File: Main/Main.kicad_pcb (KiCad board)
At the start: 2 copper layers, 32.5 x 41.5 mm, 34 parts, among them IC1 L9110S, IC2 L9110S, IC3 L9110S, J1 Conn_01x10_Female, J2 I2C_STANDARDQWIIC, J3 Conn_01x02_Female, J4 Conn_01x05_Female, J5 Conn_01x05_Female, J6 Conn_01x05_Female, J7 Conn_01x12_Female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

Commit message: change ADC's and add seconde qwiic connector
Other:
- board text added: "Main V0.1"
- board text removed: "Main"
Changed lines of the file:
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@@
     (effects (font (size 0.5 0.5) (thickness 0.1)))
   )
-  (gr_text "Main" (at 80.35 88.5) (layer "F.SilkS")
+  (gr_text "Main V0.1" (at 80.35 88.5) (layer "F.SilkS")
     (effects (font (size 1 1) (thickness 0.2)))
   )

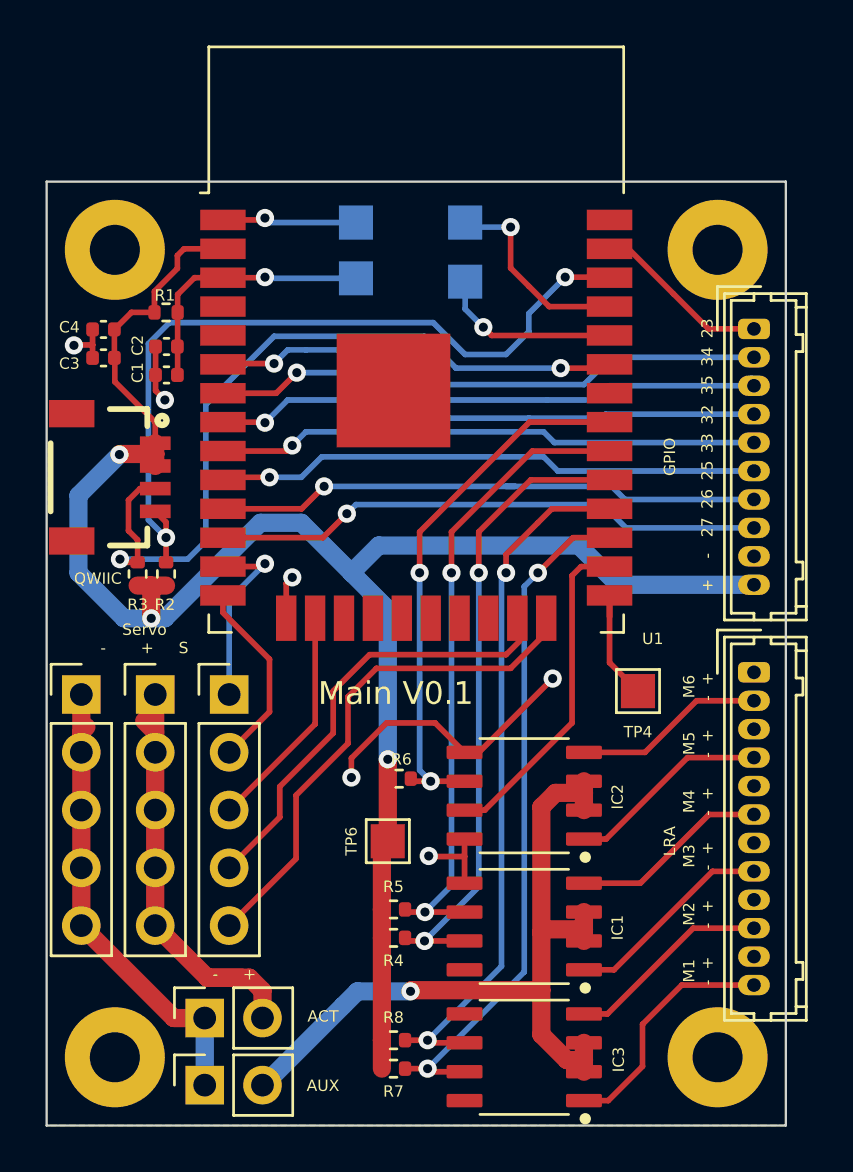
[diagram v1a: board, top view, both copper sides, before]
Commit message: main board : improve silkscreen, LCSC sourcing, capacitor value and JLCPCB files
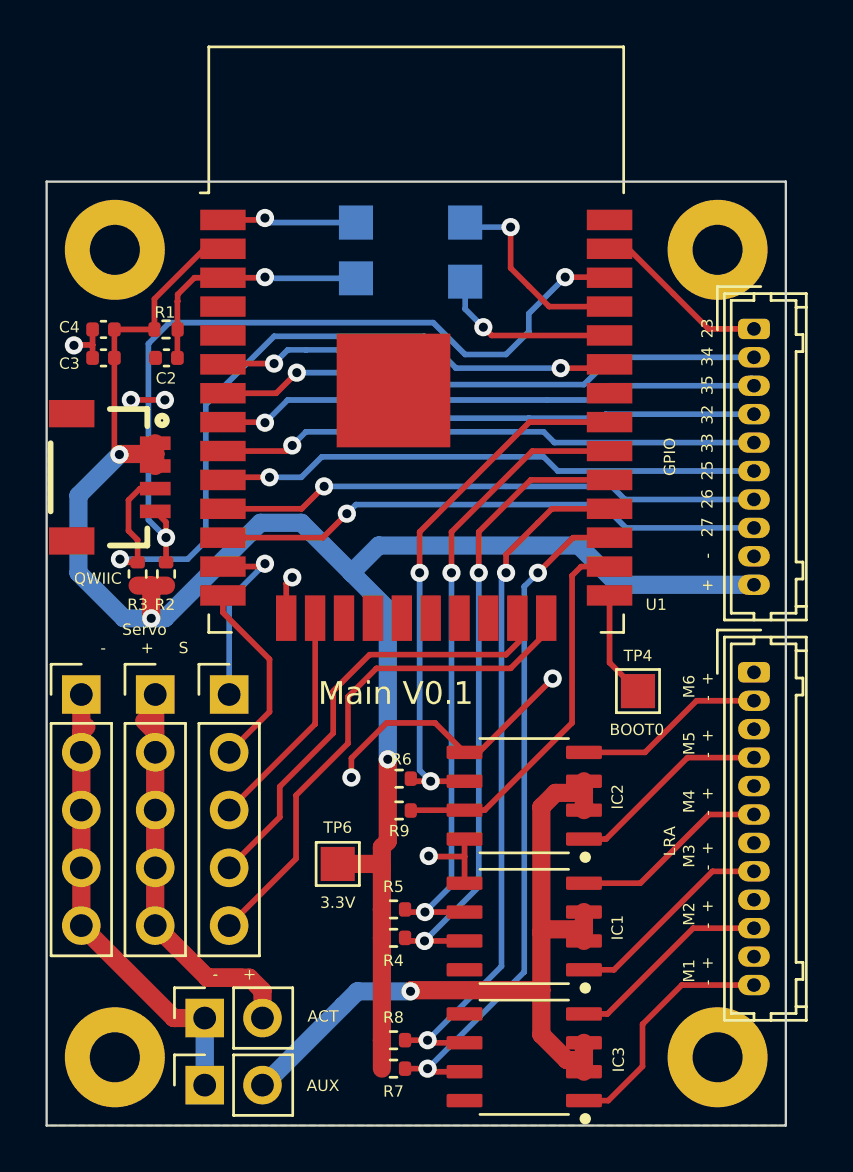
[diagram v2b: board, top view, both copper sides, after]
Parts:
- removed C1: C, Capacitor_SMD:C_0402_1005Metric
- added R9: 10K, Resistor_SMD:R_0402_1005Metric, F.Cu at (80.5, 93.7)
- C2, C4: value C -> 0.1uF
- C3: value C -> 22uF
- moved TP6 2.42 mm to (77.8, 96.0)
- moved R1 0.75 mm to (70.2, 72.5)
- moved C2 0.50 mm to (70.3, 73.8)
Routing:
- net /S11: track 14.6 -> 17.0 mm
- net +3V3: track 81.5 -> 83.2 mm
- net GND: track 49.0 -> 47.7 mm, vias 7 -> 8
- net /BOOT0: track 5.68 -> 4.72 mm
- net /EN: track 11.7 -> 11.0 mm
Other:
- board text added: "3.3V"
- board text added: "BOOT0"
- board text added: "EN"
- board text added: "GND"
- board text added: "RX0"
- board text added: "TX0"
